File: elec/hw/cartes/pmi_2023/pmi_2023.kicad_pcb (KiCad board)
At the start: 2 copper layers, 85 x 73 mm, 240 parts, among them J1 con_servo, J2 con_servo, J3 con_servo, J4 con_servo, J5 254, J7 USB4105-GF-A-060, J8 254, Q2 2N7002, Q3 DMP2008UFG-7, SW1 ESE22MH22, SW2 ESE22MH24, SW5 DS1040-04RN, SW6 2425755-1, SW7 MSS12C02LS-BB2.0, SW8 MSS12C02LS-BB2.0, U1 DRV8231ADDAR, U10 tof_sensor_master, U11 XRA1200PIG16TR-F, U12 LSM6DSO32XTR, U13 GP2S60B, U14 GP2S60B, U15 GP2S60B, U16 GP2S60B, U17 tof_sensor_master, U19 GP2S60B, U2 DRV8231ADDAR, U20 GP2S60B, U21 tof_sensor_master, U23 PCA9685PW, U24 SN74LVC1T45DBV, U25 SN74LVC1T45DBV, U26 SN74LVC1T45DBV, U27 SN74LVC1T45DBV, U28 TLV61070A, U29 TLV61070A, U3 EESX1321, U32 ESP32-S3-WROOM-1, U33 TLV61070A, U34 TLV61070A, U35 LDL1117S33R, U4 EESX1321, U5 AD8531ARTZ, U6 tof_sensor_master, U7 XRA1200PIG16TR-F, U8 GP2S60B, U9 GP2S60B

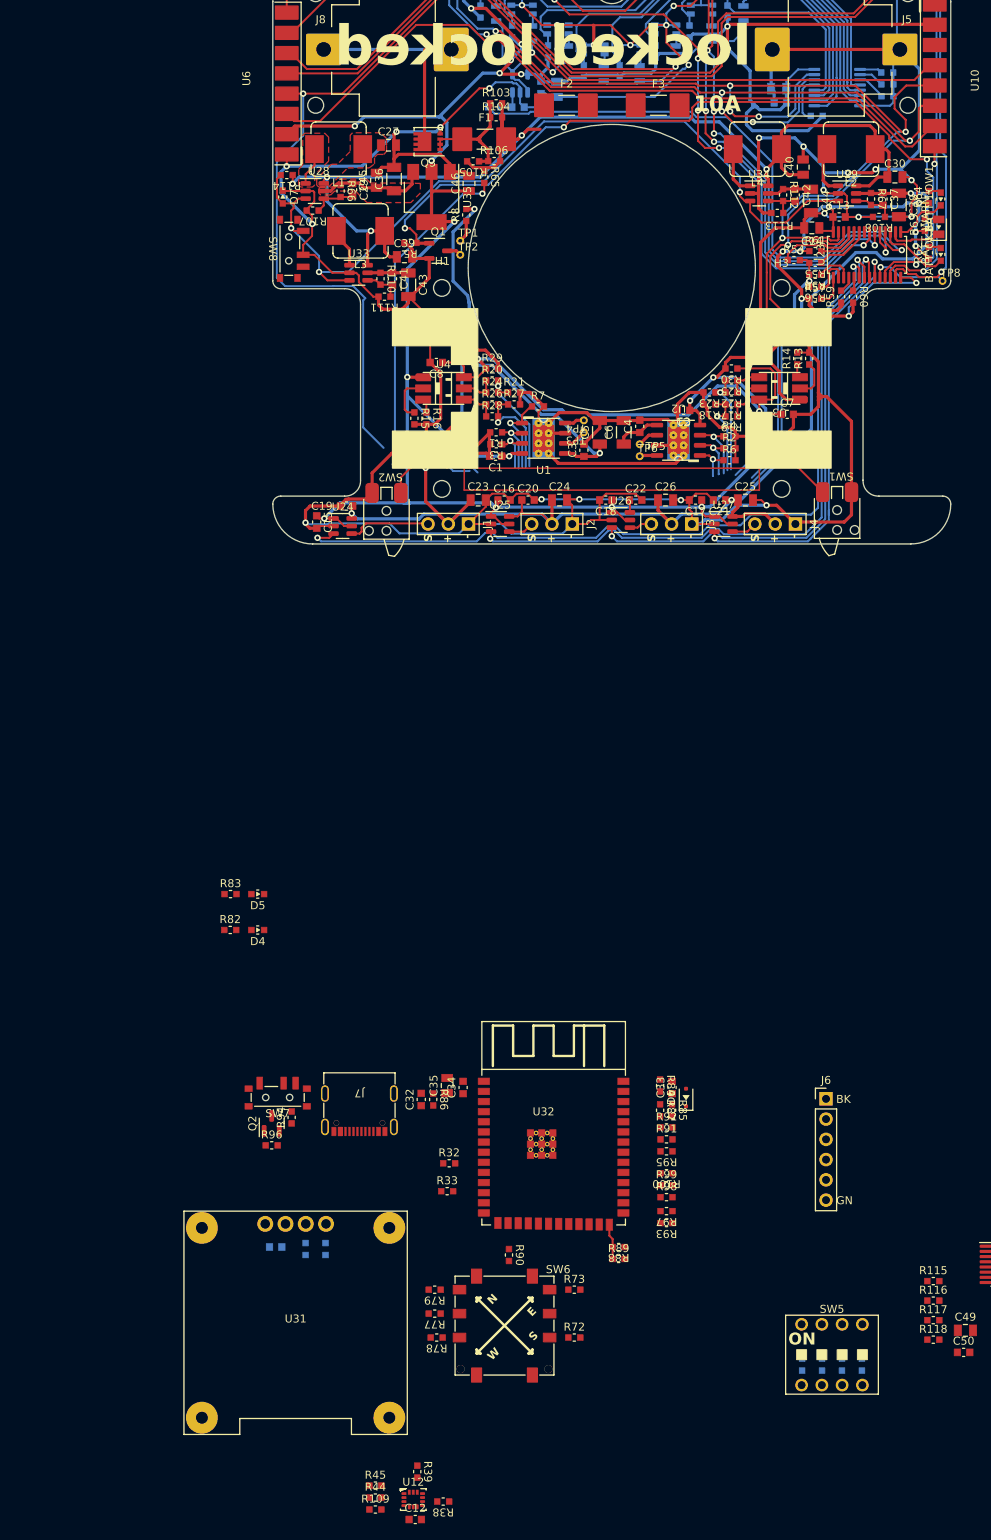
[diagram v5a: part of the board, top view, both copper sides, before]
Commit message: pmi layout (WIP)
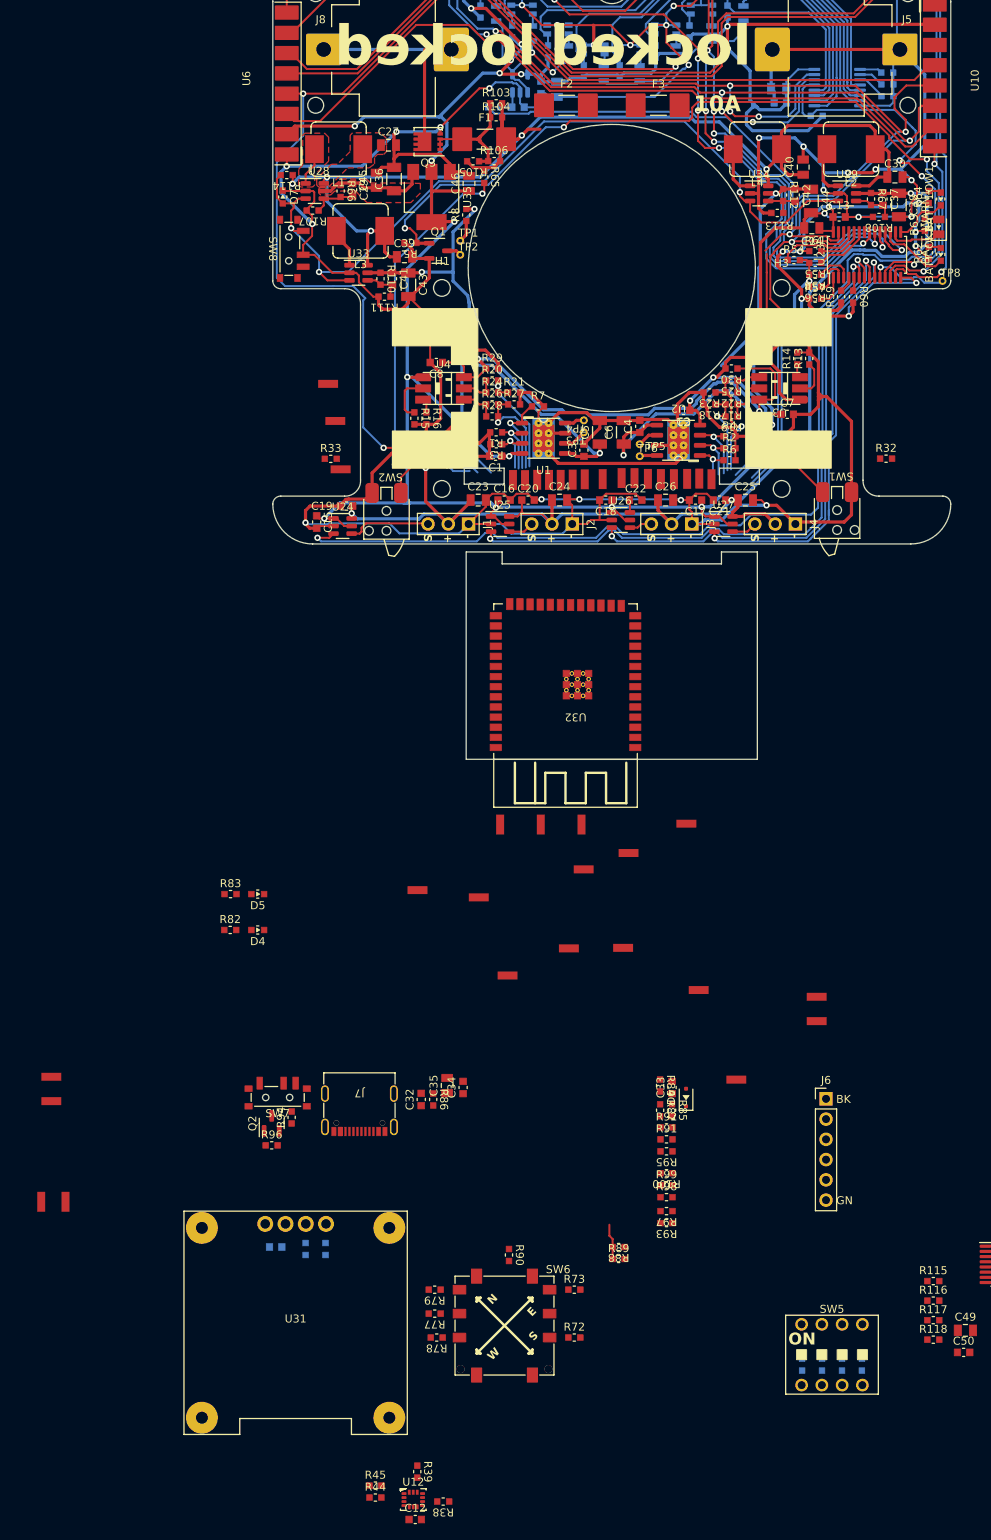
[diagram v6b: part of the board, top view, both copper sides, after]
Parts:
- removed R109: 100k, cocotter_resistor:r0603_reflow
- added J10: Conn_01x01_Pin, cocotter_others:board_to_module_small, F.Cu at (128.5, 188.2)
- added J11: Conn_01x01_Socket, cocotter_others:board_to_module_small, F.Cu at (153.5, 144.8)
- added J12: Conn_01x01_Pin, cocotter_others:board_to_module_small, F.Cu at (143.9, 203.6)
- added J13: Conn_01x01_Pin, cocotter_others:board_to_module_small, F.Cu at (137.1, 203.7)
- added J14: Conn_01x01_Socket, cocotter_others:board_to_module_small, F.Cu at (155.0, 144.9)
- added J15: Conn_01x01_Socket, cocotter_others:board_to_module_small, F.Cu at (151.9, 144.8)
- added J16: Conn_01x01_Pin, cocotter_others:board_to_module_small, F.Cu at (118.1, 196.4)
- added J17: Conn_01x01_Pin, cocotter_others:board_to_module_small, F.Cu at (168.2, 209.8)
- added J18: Conn_01x01_Pin, cocotter_others:board_to_module_small, F.Cu at (168.2, 212.8)
- added J19: Conn_01x01_Pin, cocotter_others:board_to_module_small, F.Cu at (144.6, 191.8)
- added J20: Conn_01x01_Socket, cocotter_others:board_to_module_small, F.Cu at (150.3, 144.9)
- added J21: Conn_01x01_Socket, cocotter_others:board_to_module_small, F.Cu at (133.2, 145.0)
- added J22: Conn_01x01_Socket, cocotter_others:board_to_module_small, F.Cu at (134.6, 145.0)
- added J23: Conn_01x01_Pin, cocotter_others:board_to_module_small, F.Cu at (139.0, 193.8)
- added J24: Conn_01x01_Pin, cocotter_others:board_to_module_small, F.Cu at (125.8, 197.3)
- added J25: Conn_01x01_Pin, cocotter_others:board_to_module_small, F.Cu at (72.2, 219.8)
- added J26: Conn_01x01_Pin, cocotter_others:board_to_module_small, F.Cu at (72.2, 222.9)
- added J27: Conn_01x01_Socket, cocotter_others:board_to_module_small, F.Cu at (130.1, 145.0)
- added J28: Conn_01x01_Socket, cocotter_others:board_to_module_small, F.Cu at (131.6, 145.0)
- added J29: Conn_01x01_Socket, cocotter_others:board_to_module_small, F.Cu at (147.0, 144.8)
- added J30: Conn_01x01_Socket, cocotter_others:board_to_module_small, F.Cu at (148.7, 144.9)
- added J31: Conn_01x01_Pin, cocotter_others:board_to_module_small, F.Cu at (129.4, 207.1)
- added J32: Conn_01x01_Pin, cocotter_others:board_to_module_small, F.Cu at (158.1, 220.2)
- added J33: Conn_01x01_Socket, cocotter_others:board_to_module_small, F.Cu at (137.6, 144.9)
- added J34: Conn_01x01_Socket, cocotter_others:board_to_module_small, F.Cu at (143.7, 144.7)
- added J35: Conn_01x01_Pin, cocotter_others:board_to_module_small, F.Cu at (151.8, 188.1)
- added J36: Conn_01x01_Socket, cocotter_others:board_to_module_small, F.Cu at (145.3, 144.8)
- added J37: Conn_01x01_Pin, cocotter_others:board_to_module_small, F.Cu at (153.4, 208.9)
- added J38: Conn_01x01_Socket, cocotter_others:board_to_module_small, F.Cu at (136.1, 145.0)
- added J39: Conn_01x01_Pin, cocotter_others:board_to_module_small, F.Cu at (71.0, 235.5)
- added J40: Conn_01x01_Pin, cocotter_others:board_to_module_small, F.Cu at (74.0, 235.5)
- added J41: Conn_01x01_Socket, cocotter_others:board_to_module_small, F.Cu at (141.4, 144.9)
- added J42: Conn_01x01_Socket, cocotter_others:board_to_module_small, F.Cu at (139.1, 144.9)
- added J43: Conn_01x01_Socket, cocotter_others:board_to_module_small, F.Cu at (107.8, 137.6)
- added J44: Conn_01x01_Pin, cocotter_others:board_to_module_small, F.Cu at (133.6, 188.2)
- added J45: Conn_01x01_Socket, cocotter_others:board_to_module_small, F.Cu at (106.9, 132.9)
- added J46: Conn_01x01_Pin, cocotter_others:board_to_module_small, F.Cu at (138.7, 188.2)
- added J9: Conn_01x01_Socket, cocotter_others:board_to_module_small, F.Cu at (108.5, 143.6)
- moved R32 103.9 mm to (176.9, 142.3)
- moved R33 93.0 mm to (107.3, 142.3)
- moved U32 58.4 mm to (136.7, 170.3), turned to 180 degrees
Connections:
- net /com/CAN_rx_3v3 renamed /boards interface/com/CAN_rx_3v3
- net /com/CAN_tx_3v3 renamed /boards interface/com/CAN_tx_3v3
- net /com/EN_ESP32_3v3 renamed /boards interface/com/EN_ESP32_3v3
- net /com/USB_D+ renamed /boards interface/com/USB_D+
- net /com/USB_D- renamed /boards interface/com/USB_D-
- net /com/USB_VBUS renamed /boards interface/com/USB_VBUS
- net /com/boot/dl_select_3v3 renamed /boards interface/com/boot/dl_select_3v3
- net /com/esp32_dbg_rx_3v3 renamed /boards interface/com/esp32_dbg_rx_3v3
- net /com/esp32_dbg_tx_3v3 renamed /boards interface/com/esp32_dbg_tx_3v3
- net /com/esp32_vbatt_mon_2v9 renamed /boards interface/com/esp32_vbatt_mon_2v9
- net /com/gyro_miso_3v3 renamed /boards interface/Sensor module/gyro_miso_3v3
- net /com/gyro_mosi_3v3 renamed /boards interface/Sensor module/gyro_mosi_3v3
- net /com/gyro_sck_3v3 renamed /boards interface/Sensor module/gyro_sck_3v3
- net /com/i2C_io_int_3v3 renamed /boards interface/com/i2C_io_int_3v3
- net /com/led_com_3v3 renamed /boards interface/com/led_com_3v3
- net /com/led_esp_3v3 renamed /boards interface/com/led_esp_3v3
- net /interface/conf0 renamed /boards interface/interface/conf0
- net /interface/conf1 renamed /boards interface/interface/conf1
- net /interface/conf2 renamed /boards interface/interface/conf2
- net /interface/conf3 renamed /boards interface/interface/conf3
- net /interface/esp32_scl_3v3 renamed /boards interface/interface/esp32_scl_3v3
- net /interface/esp32_sda_3v3 renamed /boards interface/interface/esp32_sda_3v3
- net /interface/select0 renamed /boards interface/interface/select0
- net /interface/select1 renamed /boards interface/interface/select1
- net /interface/select2 renamed /boards interface/interface/select2
- net /interface/select3 renamed /boards interface/interface/select3
- net /interface/select4 renamed /boards interface/interface/select4
- net /sensors/i2C_io_int_3v3 renamed /boards interface/i2C_io_int_3v3
- C12 pad 1: +3V3 -> +3V3_m
- C12 pad 2: GND -> GND_M
- C3 pad 1: /propulsion/Vmot_left_5V -> /power_supply/Vmot_left_5V
- C31 pad 1: +3V3 -> +3V3_m
- C31 pad 2: GND -> GND_M
- C32 pad 2: GND -> GND_M
- C33 pad 2: GND -> GND_M
- C34 pad 1: +3V3 -> +3V3_m
- C34 pad 2: GND -> GND_M
- C35 pad 1: +3V3 -> +3V3_m
- C35 pad 2: GND -> GND_M
- C4 pad 1: /propulsion/Vmot_right_5V -> /power_supply/Vmot_right_5V
- C49 pad 1: +3V3 -> +3V3_m
- C49 pad 2: GND -> GND_M
- C5 pad 1: /propulsion/Vmot_left_5V -> /power_supply/Vmot_left_5V
- C50 pad 1: +3V3 -> +3V3_m
- C50 pad 2: GND -> GND_M
- C6 pad 1: /propulsion/Vmot_right_5V -> /power_supply/Vmot_right_5V
- D4 pad C: GND -> GND_M
- D5 pad C: GND -> GND_M
- D6 pad 1: +3V3 -> +3V3_m
- J6 pad 1: GND -> GND_M
- J7 pad A1: GND -> GND_M
- J7 pad A12: GND -> GND_M
- J7 pad B1: GND -> GND_M
- J7 pad B12: GND -> GND_M
- J7 pad SHIELD: GND -> GND_M
- Q2 pad 2: GND -> GND_M
- R100 pad 2: /com/scl_3v3 -> /boards interface/com/scl_3v3
- R115 pad 1: +3V3 -> +3V3_m
- R116 pad 2: GND -> GND_M
- R117 pad 2: GND -> GND_M
- R118 pad 1: +3V3 -> +3V3_m
- R38 pad 1: +3V3 -> +3V3_m
- R38 pad 2: Net-(U12-INT2/DEN) -> Net-(U12-INT1)
- R39 pad 1: +3V3 -> +3V3_m
- R39 pad 2: /com/gyro_ncs_3v3 -> Net-(U12-INT2/DEN)
- R44 pad 1: +3V3 -> +3V3_m
- R44 pad 2: Net-(U12-SCx) -> /boards interface/Sensor module/gyro_ncs_3v3
- R45 pad 1: +3V3 -> +3V3_m
- R45 pad 2: Net-(U12-SDx) -> Net-(U12-SCx)
- R6 pad 1: /com/i_prop_right_3v3 -> /boards interface/i_prop_right_3v3
- R65 pad 2: /com/vbatt_mon_4.35V -> /power_supply/vbatt_mon_4.35V
- R68 pad 2: GND -> GND_M
- R69 pad 2: GND -> GND_M
- R7 pad 1: /com/i_prop_left_3v3 -> /boards interface/i_prop_left_3v3
- R70 pad 2: GND -> GND_M
- R71 pad 2: GND -> GND_M
- R72 pad 2: GND -> GND_M
- R73 pad 2: GND -> GND_M
- R74 pad 1: /actuators/LED_RGB_R_3v3 -> /LED_RGB_R_3v3
- R75 pad 1: /actuators/LED_RGB_G_3v3 -> /LED_RGB_B_3v3
- R75 pad 2: Net-(D1-C_GREEN) -> Net-(D1-C_BLUE)
- R76 pad 1: /actuators/LED_RGB_B_3v3 -> /LED_RGB_G_3v3
- R76 pad 2: Net-(D1-C_BLUE) -> Net-(D1-C_GREEN)
- R77 pad 2: GND -> GND_M
- R78 pad 2: GND -> GND_M
- R79 pad 2: GND -> GND_M
- R8 pad 2: /propulsion/Vmot_left_5V -> /power_supply/Vmot_left_5V
- R80 pad 1: +3V3 -> +3V3_m
- R81 pad 1: +3V3 -> +3V3_m
- R84 pad 1: GND -> GND_M
- R85 pad 2: /com/vbatt_mon_4.35V -> /boards interface/com/vbatt_mon_4.35V
- R86 pad 1: +3V3 -> +3V3_m
- R87 pad 2: /com/vbatt_mon_4.35V -> /boards interface/com/vbatt_mon_4.35V
- R88 pad 1: +3V3 -> +3V3_m
- R89 pad 2: GND -> GND_M
- R90 pad 2: GND -> GND_M
- R93 pad 1: +3V3 -> +3V3_m
- R95 pad 1: +3V3 -> +3V3_m
- R96 pad 2: GND -> GND_M
- R97 pad 2: /com/sda_3v3 -> /boards interface/com/sda_3v3
- R98 pad 1: +3V3 -> +3V3_m
- R99 pad 1: +3V3 -> +3V3_m
- SW5 pad 5: +3V3 -> +3V3_m
- SW5 pad 6: +3V3 -> +3V3_m
- SW5 pad 7: +3V3 -> +3V3_m
- SW5 pad 8: +3V3 -> +3V3_m
- SW6 pad 5: +3V3 -> +3V3_m
- U1 pad 1: /com/i_prop_left_3v3 -> /boards interface/i_prop_left_3v3
- U1 pad 5: /propulsion/Vmot_left_5V -> /power_supply/Vmot_left_5V
- U10 pad 5: /com/sda_3v3 -> /boards interface/sda_3v3
- U10 pad 6: /com/scl_3v3 -> /boards interface/scl_3v3
- U11 pad 14: /com/scl_3v3 -> /boards interface/com/scl_3v3
- U11 pad 15: /com/sda_3v3 -> /boards interface/com/sda_3v3
- U11 pad 16: +3V3 -> +3V3_m
- U11 pad 8: GND -> GND_M
- U12 pad 12: /com/gyro_ncs_3v3 -> /boards interface/Sensor module/gyro_ncs_3v3
- U12 pad 5: +3V3 -> +3V3_m
- U12 pad 6: GND -> GND_M
- U12 pad 7: GND -> GND_M
- U12 pad 8: +3V3 -> +3V3_m
- U17 pad 5: /com/sda_3v3 -> /boards interface/sda_3v3
- U17 pad 6: /com/scl_3v3 -> /boards interface/scl_3v3
- U2 pad 1: /com/i_prop_right_3v3 -> /boards interface/i_prop_right_3v3
- U2 pad 5: /propulsion/Vmot_right_5V -> /power_supply/Vmot_right_5V
- U21 pad 5: /com/sda_3v3 -> /boards interface/sda_3v3
- U21 pad 6: /com/scl_3v3 -> /boards interface/scl_3v3
- U23 pad 26: /com/scl_3v3 -> /boards interface/scl_3v3
- U23 pad 27: /com/sda_3v3 -> /boards interface/sda_3v3
- U31 pad 1: GND -> GND_M
- U31 pad 2: +3V3 -> +3V3_m
- U32 pad 1: GND -> GND_M
- U32 pad 12: /propulsion/dir_right -> /boards interface/com/pwm_right
- U32 pad 15: /com/i_prop_right_3v3 -> /boards interface/com/i_prop_right_3v3
- U32 pad 17: /propulsion/pwm_right -> /boards interface/com/dir_right
- U32 pad 18: /com/gyro_ncs_3v3 -> /boards interface/Sensor module/gyro_ncs_3v3
- U32 pad 2: +3V3 -> +3V3_m
- U32 pad 24: /sensors/tof_irq -> /boards interface/com/tof_irq
- U32 pad 29: /com/sda_3v3 -> /boards interface/com/sda_3v3
- U32 pad 30: /com/scl_3v3 -> /boards interface/com/scl_3v3
- U32 pad 32: /propulsion/right_encod_B_3v3 -> /boards interface/com/right_encod_B_3v3
- U32 pad 33: /propulsion/right_encod_A_3v3 -> /boards interface/com/right_encod_A_3v3
- U32 pad 34: /propulsion/left_encod_B_3v3 -> /boards interface/com/left_encod_B_3v3
- U32 pad 35: /propulsion/left_encod_A_3v3 -> /boards interface/com/left_encod_A_3v3
- U32 pad 38: /com/i_prop_left_3v3 -> /boards interface/com/i_prop_left_3v3
- U32 pad 40: GND -> GND_M
- U32 pad 41: GND -> GND_M
- U32 pad 6: /propulsion/pwm_left -> /boards interface/com/pwm_left
- U32 pad 7: /propulsion/dir_left -> /boards interface/com/dir_left
- U32 pad 8: /sensors/ctc_right -> /boards interface/com/ctc_right
- U32 pad 9: /sensors/ctc_left -> /boards interface/com/ctc_left
- U6 pad 5: /com/sda_3v3 -> /boards interface/sda_3v3
- U6 pad 6: /com/scl_3v3 -> /boards interface/scl_3v3
- U7 pad 14: /com/scl_3v3 -> /boards interface/scl_3v3
- U7 pad 15: /com/sda_3v3 -> /boards interface/sda_3v3
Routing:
- net /com/sda_3v3: track 188.6 -> 0.00 mm, vias 8 -> 0
- net /com/scl_3v3: track 185.6 -> 0.00 mm, vias 8 -> 0
- net /boards interface/scl_3v3: track 0.00 -> 185.0 mm, vias 0 -> 8
- net /boards interface/sda_3v3: track 0.00 -> 158.1 mm, vias 0 -> 7
- net /boards interface/i2C_io_int_3v3: track 5.87 -> 77.5 mm, vias 0 -> 2
- net /power_supply/Vmot_right_5V: track 5.60 -> 75.5 mm, vias 0 -> 4
- net /power_supply/Vmot_left_5V: track 5.12 -> 65.6 mm, vias 0 -> 3
- net /propulsion/Vmot_left_5V: track 53.7 -> 0.00 mm, vias 2 -> 0
- net /power_supply/vbatt_mon_4.35V: track 0.00 -> 52.9 mm, vias 0 -> 3
- net /com/vbatt_mon_4.35V: track 52.9 -> 0.00 mm, vias 3 -> 0
- net (no net): track 0.00 -> 30.0 mm, vias 0 -> 1
- net /sensors/tof_irq: track 148.7 -> 163.4 mm, vias 1 -> 3
- net /com/i_prop_left_3v3: track 10.4 -> 0.00 mm, vias 1 -> 0
- net /boards interface/i_prop_left_3v3: track 0.00 -> 10.4 mm, vias 0 -> 1
- net /propulsion/Vmot_right_5V: track 5.68 -> 0.00 mm
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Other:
- board size 85 x 73 mm -> 85 x 100 mm
